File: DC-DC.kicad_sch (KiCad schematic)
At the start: 16 parts

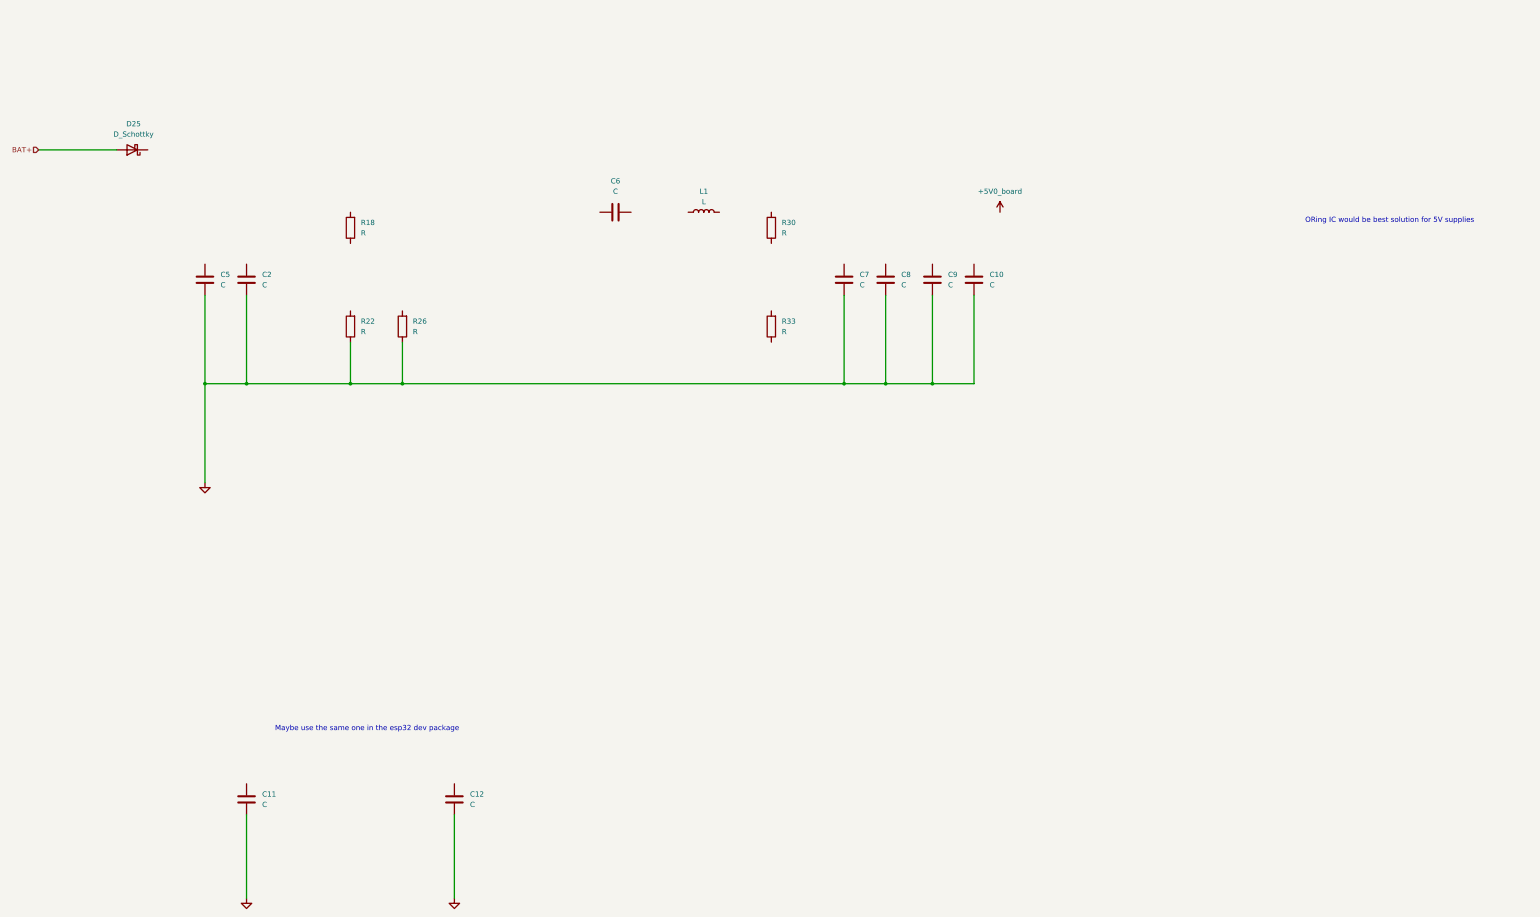
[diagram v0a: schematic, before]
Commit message: Worked on the MCU page and the DC-DC page. Will still need to change a few things and add the buzzer and piezo stuff (#3)
Co-authored-by: Nima <nima.shirazi@flyzipline.com>
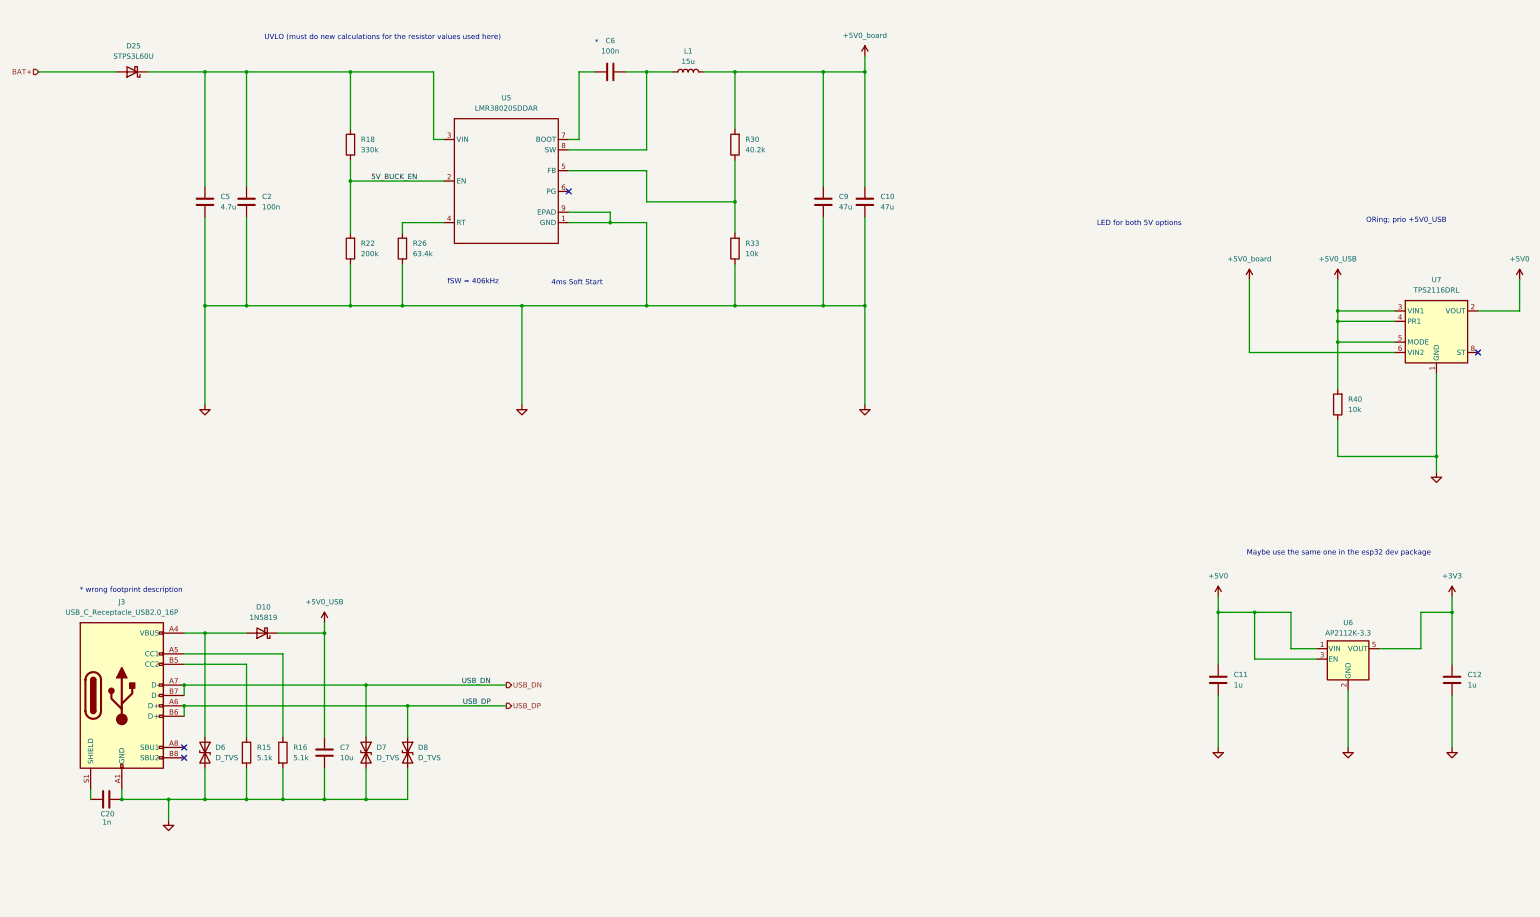
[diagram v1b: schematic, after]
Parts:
- removed C8: C, symbol Device:C
- added C20: 1n, symbol Device:C
- added D10: 1N5819, custom_footprints:1N5819HW-7-F, symbol Diode:1N5819
- added D6, D7, D8: D_TVS, Diode_SMD:D_0402_1005Metric, symbol Device:D_TVS
- added J3: USB_C_Receptacle_USB2.0_16P, Connector_USB:USB_C_Receptacle_GCT_USB4105-xx-A_16P_TopMnt_Horizontal, symbol Connector:USB_C_Receptacle_USB2.0_16P
- added R15, R16: 5.1k, symbol Device:R
- added R40: 10k, symbol Device:R
- added U5: LMR38020SDDAR, Package_SO:Texas_R-PDSO-G8_EP2.95x4.9mm_Mask2.4x3.1mm, symbol custom_symbols:LMR38020SDDAR
- added U6: AP2112K-3.3, Package_TO_SOT_SMD:SOT-23-5, symbol Regulator_Linear:AP2112K-3.3
- added U7: TPS2116DRL, Package_TO_SOT_SMD:SOT-583-8, symbol Power_Management:TPS2116DRL
- C10, C9: value C -> 47u
- C11, C12: value C -> 1u
- C2, C6: value C -> 100n
- C5: value C -> 4.7u
- C7: value C -> 10u
- D25: value D_Schottky -> STPS3L60U; footprint (none) -> custom_footprints:STPS3L60U
- L1: value L -> 15u; footprint (none) -> Inductor_SMD:L_Bourns_SRR1208_12.7x12.7mm
- R18: value R -> 330k
- R22: value R -> 200k
- R26: value R -> 63.4k
- R30: value R -> 40.2k
- R33: value R -> 10k
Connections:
- net +5V0_board: now also C10.1, C9.1, L1.2, R30.2, U7.6 (VIN2)
- net GND: now also C7.1, R33.1, C20.2, D6.2 (A2), D7.2 (A2), D8.2 (A2), J3.A1 (GND), J3.A12 (GND), J3.B1 (GND), J3.B12 (GND), R15.2, R16.2, R40.1, U5.1 (GND), U5.9 (EPAD), U6.2 (GND), U7.1 (GND); no longer C7.2
- net at C2.1: now also C5.1, D25.1 (K), R18.2, U5.3 (VIN)
- net at R33.2: now also R30.1, U5.5 (FB)
- net at C6.1: now also L1.1, U5.8 (SW)
- net at C6.2: now also U5.7 (BOOT)
- net +3V3: now reaches C12.1
- net +3V3: now also U6.5 (VOUT)
- net at R26.2: now also U5.4 (RT)
- net 5V_BUCK_EN: now reaches R22.2
- net 5V_BUCK_EN: now also R18.1, U5.2 (EN)
- net +5V0: now reaches C11.1
- net +5V0: now also U6.1 (VIN), U6.3 (EN), U7.2 (VOUT), U7.7 (VOUT)
- new net: D10.2 (A), D6.1 (A1), J3.A4 (VBUS), J3.A9 (VBUS), J3.B4 (VBUS), J3.B9 (VBUS)
- new net: J3.A5 (CC1), R16.1
- new net: J3.B5 (CC2), R15.1
- new net: C20.1, J3.S1 (SHIELD)
- new net +5V0_USB: C7.2, D10.1 (K), R40.2, U7.3 (VIN1), U7.4 (PR1), U7.5 (MODE)
- new net USB_DN: D7.1 (A1), J3.A7 (D-), J3.B7 (D-)
- new net USB_DP: D8.1 (A1), J3.A6 (D+), J3.B6 (D+)
- no-connect marks 0 -> 4
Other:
- note added: "*"
- note added: "* wrong footprint description"
- note added: "4ms Soft Start"
- note added: "LED for both 5V options"
- note added: "ORing; prio +5V0_USB"
- note added: "UVLO (must do new calculations for the resistor values used here)"
- note added: "fSW = 406kHz"
- note removed: "ORing IC would be best solution for 5V supplies"
- moved on the sheet: C10, C11, C12, C2, C5, C6, C9, D25, L1, R18, R22, R26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

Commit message: Added footprints to resistors and capacitors, and fixed the mosfets wiring issue (#4)
Jul9th push. Added footprints to resistors and capacitors, and fixed the mosfets wiring issue
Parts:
- C10, C11, C12, C2, C20, C5, C6, C7, C9: footprint (none) -> Capacitor_SMD:C_0603_1608Metric
- R15, R16, R18, R22, R26, R30, R33, R40: footprint (none) -> Resistor_SMD:R_0603_1608Metric
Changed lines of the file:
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@@
 			)
 		)
-		(property "Footprint" ""
+		(property "Footprint" "Resistor_SMD:R_0603_1608Metric"
 			(at 197.358 93.98 90)
 			(effects
@@
 			)
 		)
-		(property "Footprint" ""
+		(property "Footprint" "Capacitor_SMD:C_0603_1608Metric"
 			(at 161.29 51.7652 0)
 			(effects
@@
 			)
 		)
-		(property "Footprint" ""
+		(property "Footprint" "Capacitor_SMD:C_0603_1608Metric"
 			(at 371.8052 203.2 0)
 			(effects
@@
 			)
 		)
-		(property "Footprint" ""
+		(property "Footprint" "Resistor_SMD:R_0603_1608Metric"
 			(at 344.678 132.08 90)
 			(effects
@@
 			)
 		)
-		(property "Footprint" ""
+		(property "Footprint" "Capacitor_SMD:C_0603_1608Metric"
 			(at 45.72 227.6348 0)
 			(effects
@@
 			)
 		)
-		(property "Footprint" ""
+		(property "Footprint" "Resistor_SMD:R_0603_1608Metric"
 			(at 116.078 93.98 90)
 			(effects
@@
 			)
 		)
-		(property "Footprint" ""
+		(property "Footprint" "Capacitor_SMD:C_0603_1608Metric"
 			(at 218.1352 86.36 0)
 			(effects
@@
 			)
 		)
-		(property "Footprint" ""
+		(property "Footprint" "Resistor_SMD:R_0603_1608Metric"
 			(at 103.378 93.98 90)
 			(effects
@@
 			)
 		)
-		(property "Footprint" ""
+		(property "Footprint" "Capacitor_SMD:C_0603_1608Metric"
 			(at 77.1652 86.36 0)
 			(effects
@@
 			)
 		)
-		(property "Footprint" ""
+		(property "Footprint" "Capacitor_SMD:C_0603_1608Metric"
 			(at 314.6552 203.2 0)
 			(effects
@@
 			)
 		)
-		(property "Footprint" ""
+		(property "Footprint" "Resistor_SMD:R_0603_1608Metric"
 			(at 74.422 217.17 90)
 			(effects
@@
 			)
 		)
-		(property "Footprint" ""
+		(property "Footprint" "Resistor_SMD:R_0603_1608Metric"
 			(at 103.378 68.58 90)
 			(effects
@@
 			)
 		)
-		(property "Footprint" ""
+		(property "Footprint" "Resistor_SMD:R_0603_1608Metric"
 			(at 83.312 217.17 90)
 			(effects
@@
 			)
 		)
-		(property "Footprint" ""
+		(property "Footprint" "Capacitor_SMD:C_0603_1608Metric"
 			(at 94.2848 213.36 0)
 			(effects
@@
 			)
 		)
-		(property "Footprint" ""
+		(property "Footprint" "Capacitor_SMD:C_0603_1608Metric"
 			(at 228.2952 86.36 0)
 			(effects
@@
 			)
 		)
-		(property "Footprint" ""
+		(property "Footprint" "Resistor_SMD:R_0603_1608Metric"
 			(at 197.358 68.58 90)
 			(effects
@@
 			)
 		)
-		(property "Footprint" ""
+		(property "Footprint" "Capacitor_SMD:C_0603_1608Metric"
 			(at 67.0052 86.36 0)
 			(effects

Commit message: finish schematic
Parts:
- C10: renamed from C12; value 1u -> 1uF
- C9: renamed from C11; value 1u -> 1uF
- renumbered C20 to C2, C5 to C3, C2 to C4, C7 to C5, C9 to C7, C10 to C8, D25 to D10, D6 to D11, D10 to D12, D7 to D13, D8 to D14, R18 to R17, R22 to R18, R26 to R19, R30 to R20, R33 to R21, R40 to R22, U5 to U1, U6 to U2, U7 to U3
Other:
- note added: "ORing; prio +5V0_USB Switches to +5V0_board IF: +5V0_USB < 1.0V and +5V0_board >= 1.6V"
- note removed: "ORing; prio +5V0_USB"

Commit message: Did some more routing
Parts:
- R17: value 330k -> 649k
- R19: value 63.4k -> 64.9k
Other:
- note added: "3.8V-6V -> 3.3V @ 600mA"
- note added: "6V-80V -> 5V @ 2A"
- note removed: "LED for both 5V options"
- note removed: "Maybe use the same one in the esp32 dev package"
- note removed: "UVLO (must do new calculations for the resistor values used here)"
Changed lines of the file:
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@@
 		(rev "R2.0.0")
 	)
+	(text "3.8V-6V -> 3.3V @ 600mA"
+		(exclude_from_sim no)
+		(at 342.138 166.624 0)
+		(effects
+			(font
+				(size 2.54 2.54)
+				(thickness 0.3175)
+			)
+		)
+	)
 	(text "ORing; prio +5V0_USB\nSwitches to +5V0_board IF:\n+5V0_USB < 1.0V and +5V0_board >= 1.6V"
 		(exclude_from_sim no)
@@
 		)
 	)
-	(text "UVLO (must do new calculations for the resistor values used here)"
-		(exclude_from_sim no)
-		(at 109.474 42.418 0)
-		(effects
-			(font
-				(size 1.27 1.27)
-			)
-		)
-	)
-	(text "Maybe use the same one in the esp32 dev package"
+	(text "6V-80V -> 5V @ 2A"
 		(exclude_from_sim no)
-		(at 343.154 168.402 0)
+		(at 120.142 38.1 0)
 		(effects
 			(font
-				(size 1.27 1.27)
+				(size 2.54 2.54)
+				(thickness 0.3175)
 			)
 		)
@@
 		)
 	)
-	(text "LED for both 5V options "
-		(exclude_from_sim no)
-		(at 294.386 87.884 0)
-		(effects
-			(font
-				(size 1.27 1.27)
-			)
-		)
-	)
 	(junction
 		(at 66.04 187.96)
@@
 			)
 		)
-		(property "Value" "63.4k"
+		(property "Value" "64.9k"
 			(at 116.84 95.2499 0)
 			(effects
@@
 			)
 		)
-		(property "Value" "330k"
+		(property "Value" "649k"
 			(at 104.14 69.8499 0)
 			(effects
@@
 		)
 		(property "Value" "+5V0_board"
-			(at 321.31 96.52 0)
+			(at 323.85 100.3299 0)
 			(effects
 				(font
 					(size 1.27 1.27)
 				)
+				(justify left)
 			)
 		)

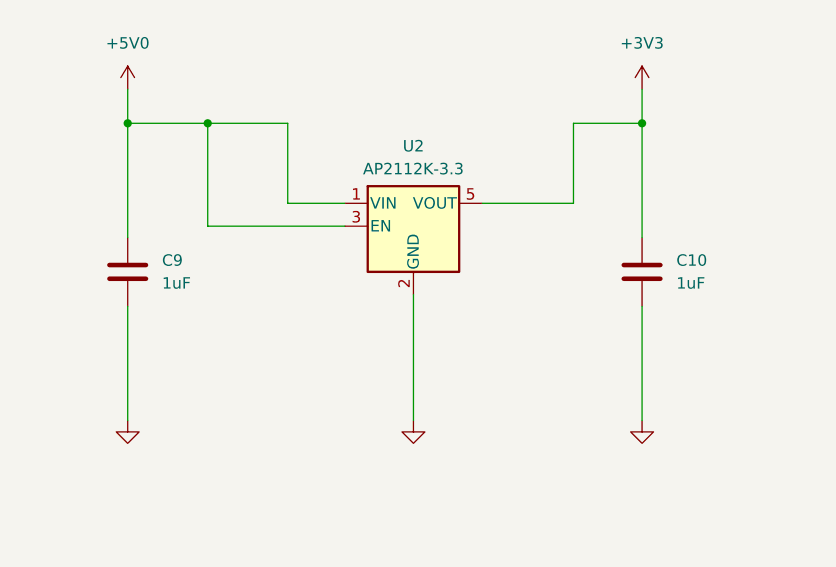
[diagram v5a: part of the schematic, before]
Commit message: More routing, changed the footprints of some caps.
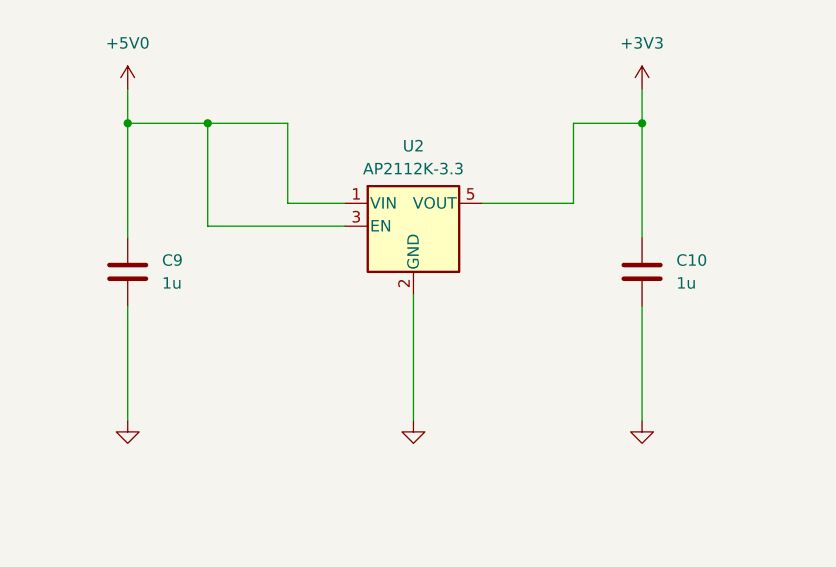
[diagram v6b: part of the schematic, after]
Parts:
- C10, C9: value 1uF -> 1u
- C3: footprint Capacitor_SMD:C_0603_1608Metric -> Capacitor_SMD:C_1206_3216Metric
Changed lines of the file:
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@@
 			(justify right bottom)
 		)
+		(property "Netclass" "90R"
+			(at 125.73 199.644 0)
+			(effects
+				(font
+					(size 1.27 1.27)
+					(italic yes)
+				)
+				(justify right)
+			)
+		)
 	)
 	(label "USB_DP"
@@
 			(justify right bottom)
 		)
+		(property "Netclass" "90R"
+			(at 125.984 204.724 0)
+			(effects
+				(font
+					(size 1.27 1.27)
+					(italic yes)
+				)
+				(justify right)
+			)
+		)
 	)
 	(hierarchical_label "USB_DN"
@@
 			)
 		)
-		(property "Value" "1uF"
+		(property "Value" "1u"
 			(at 374.65 200.6599 0)
 			(effects
@@
 			)
 		)
-		(property "Value" "1uF"
+		(property "Value" "1u"
 			(at 317.5 200.6599 0)
 			(effects
@@
 			)
 		)
-		(property "Footprint" "Capacitor_SMD:C_0603_1608Metric"
+		(property "Footprint" "Capacitor_SMD:C_1206_3216Metric"
 			(at 67.0052 86.36 0)
 			(effects

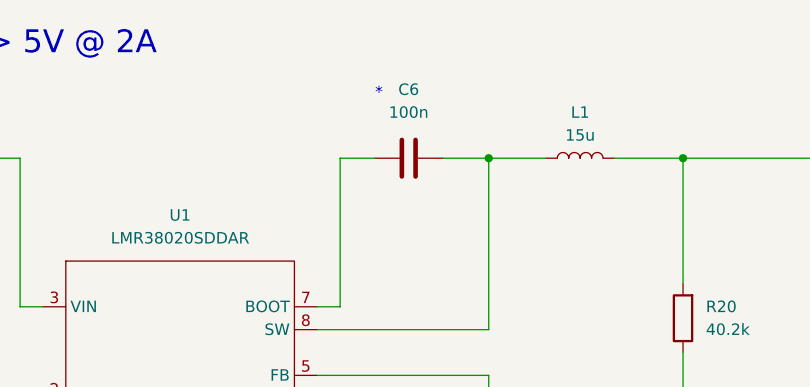
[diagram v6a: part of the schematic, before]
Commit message: Finished Routing and ran DRC. Will need final review of schematics and layout with Austin. Will also need to update BOM.
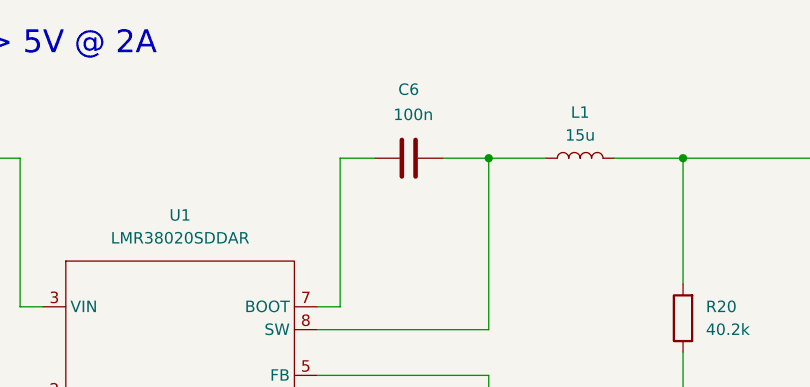
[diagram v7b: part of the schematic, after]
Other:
- note removed: "*"
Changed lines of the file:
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@@
-		)
-	)
-	(text "*"
-		(exclude_from_sim no)
-		(at 161.798 43.688 0)
-		(effects
-			(font
-				(size 1.27 1.27)
-			)
 		)
 	)
@@
 		(on_board yes)
 		(dnp no)
-		(fields_autoplaced yes)
 		(property "Reference" "C6"
 			(at 165.1 43.18 90)
@@
 		)
 		(property "Value" "100n"
-			(at 165.1 45.72 90)
+			(at 165.608 45.974 90)
 			(effects
 				(font

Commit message: add manufacturer, mpn, and package to bom
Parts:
- C10, C9: Manufacturer_Name (none) -> Taiyo Yuden; Manufacturer_Part_Number (none) -> TMK107B7105KA-T; Package (none) -> 603
- C2: Manufacturer_Name (none) -> KEMET; Manufacturer_Part_Number (none) -> C0603C102K5RACTU; Package (none) -> 603
- C3: Manufacturer_Name (none) -> Murata Electronics; Manufacturer_Part_Number (none) -> GRM31CC72A475KE11L; Package (none) -> 1206
- C4, C6: Manufacturer_Name (none) -> Samsung Electro-Mechanics; Manufacturer_Part_Number (none) -> CL10B104KC8NNNC; Package (none) -> 603
- C5: Manufacturer_Name (none) -> Taiyo Yuden; Manufacturer_Part_Number (none) -> LMK107BBJ106MALT; Package (none) -> 603
- C7, C8: Manufacturer_Name (none) -> Murata Electronics; Manufacturer_Part_Number (none) -> GRM188R60J476ME15D; Package (none) -> 603
- D10: Manufacturer_Name (none) -> STMicroelectronics; Manufacturer_Part_Number (none) -> STPS3L60U; Package (none) -> SMB
- D11, D13, D14: Manufacturer_Name (none) -> Diodes Incorporated; Manufacturer_Part_Number (none) -> D5V0H1B2LP-7B; Package (none) -> 402
- D12: Manufacturer_Name (none) -> Diodes Incorporated; Manufacturer_Part_Number (none) -> 1N5819HW-7-F; Package (none) -> SOD-123
- J3: Manufacturer_Name (none) -> GCT; Manufacturer_Part_Number (none) -> USB4105-GF-A; Package (none) -> SMT 16P
- L1: Manufacturer_Name (none) -> Bourns Inc.; Manufacturer_Part_Number (none) -> SRR1208-150ML; Package (none) -> Nonstandard
- R15, R16: Manufacturer_Name (none) -> YAGEO; Manufacturer_Part_Number (none) -> RC0603FR-075K1L; Package (none) -> 603
- R17: Manufacturer_Name (none) -> YAGEO; Manufacturer_Part_Number (none) -> RC0603FR-07649KL; Package (none) -> 603
- R18: Manufacturer_Name (none) -> YAGEO; Manufacturer_Part_Number (none) -> RC0603FR-07200KL; Package (none) -> 603
- R19: Manufacturer_Name (none) -> YAGEO; Manufacturer_Part_Number (none) -> RC0603FR-0764K9L; Package (none) -> 603
- R20: Manufacturer_Name (none) -> YAGEO; Manufacturer_Part_Number (none) -> RC0603FR-1340K2L; Package (none) -> 603
- R21, R22: Manufacturer_Name (none) -> YAGEO; Manufacturer_Part_Number (none) -> RC0603JR-0710KL; Package (none) -> 603
- U1: Manufacturer_Name (none) -> Texas Instruments; Manufacturer_Part_Number (none) -> LMR38020SDDAR; Package (none) -> 8-pin HSOIC PowerPAD
- U2: Manufacturer_Name (none) -> Diodes Incorporated; Manufacturer_Part_Number (none) -> AP2112K-3.3TRG1; Package (none) -> SOT-25
- U3: Manufacturer_Name (none) -> Texas Instruments; Manufacturer_Part_Number (none) -> TPS2116DRLR; Package (none) -> SOT-583
